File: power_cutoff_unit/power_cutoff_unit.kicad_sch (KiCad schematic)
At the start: 0 parts

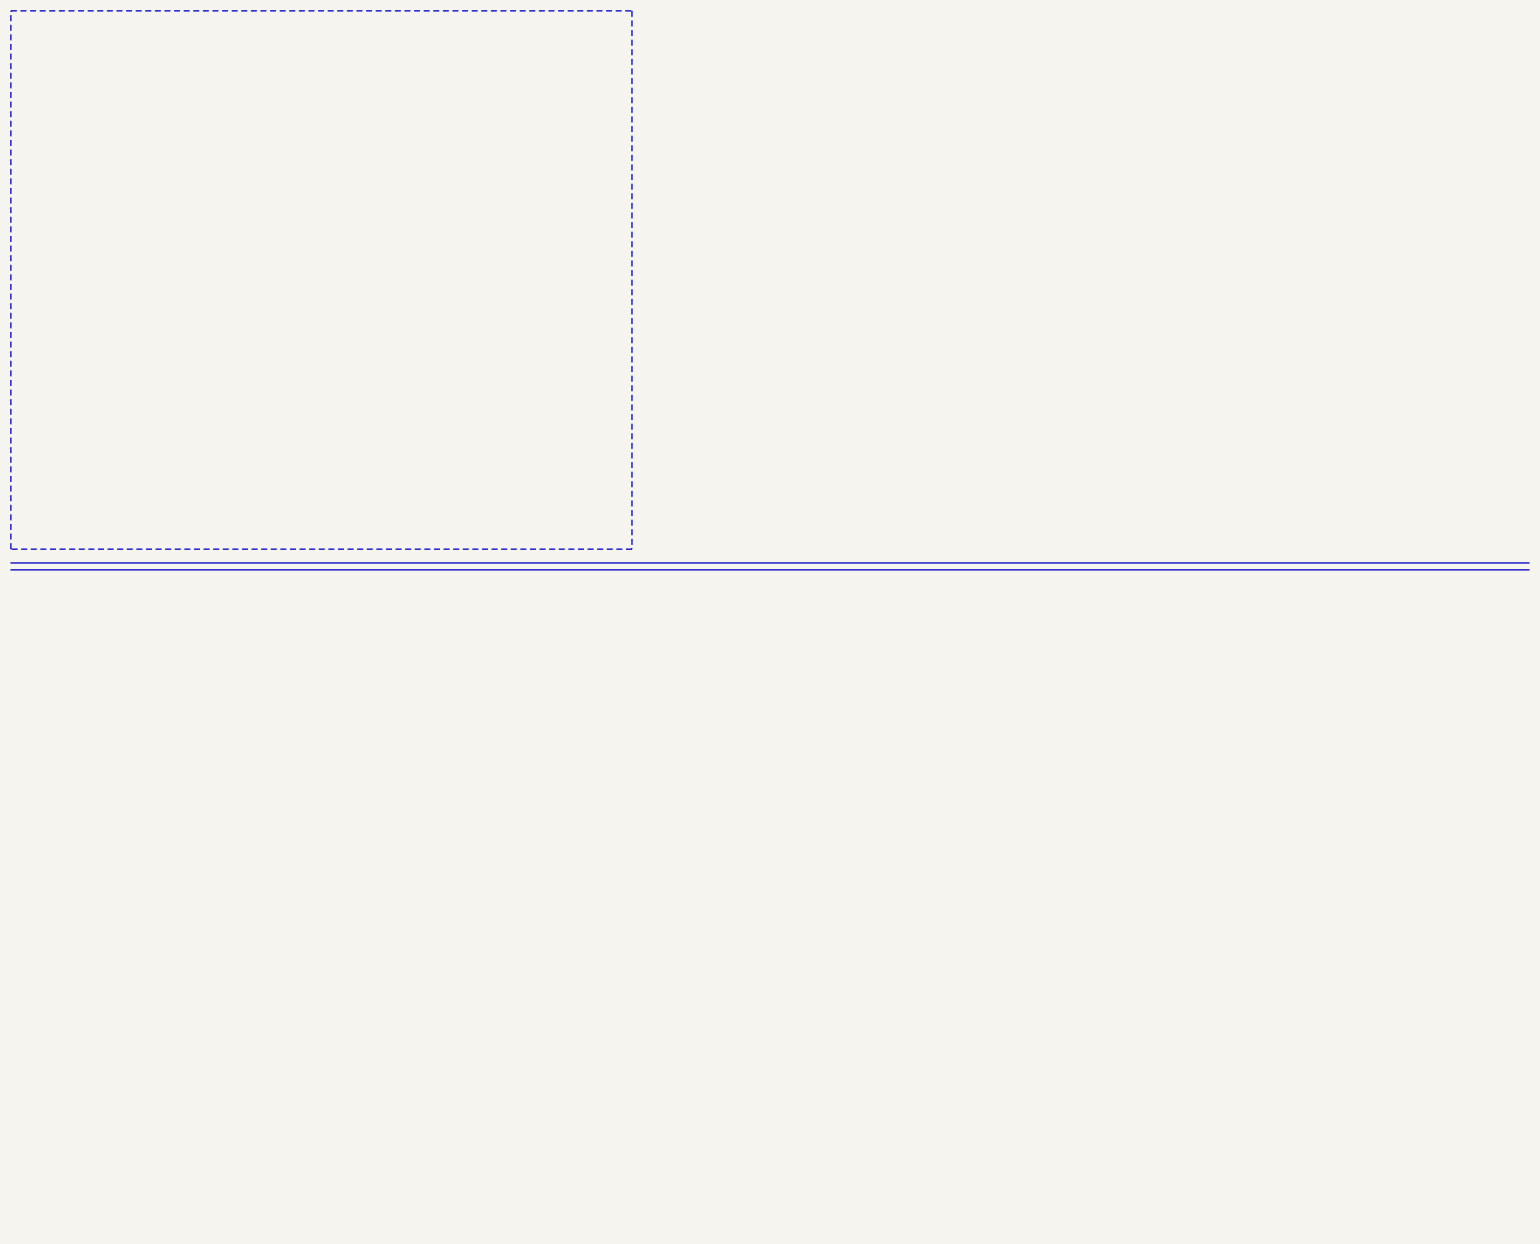
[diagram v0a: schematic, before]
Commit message: 集積回路だけ追加
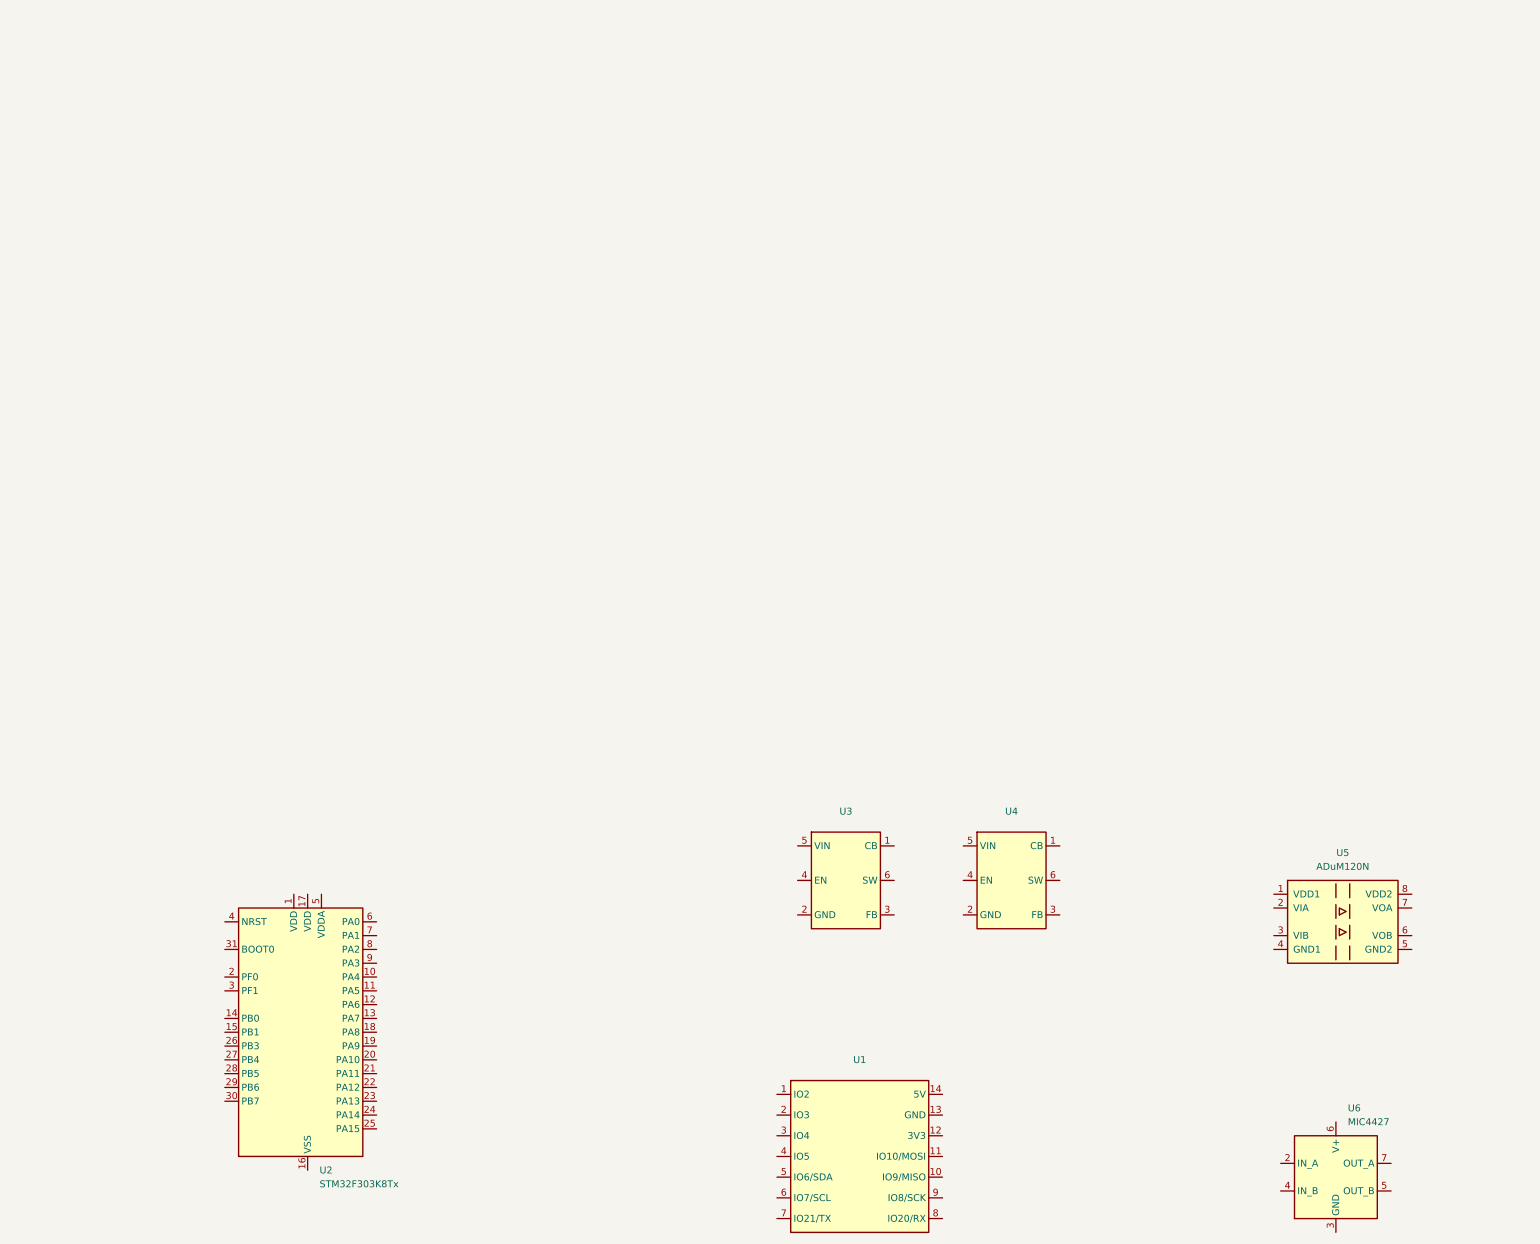
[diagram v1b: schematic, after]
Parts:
- added U1: ~, symbol Seed_XIAO:XIAO_ESP32C3
- added U2: STM32F303K8Tx, Package_QFP:LQFP-32_7x7mm_P0.8mm, symbol MCU_ST_STM32F3:STM32F303K8Tx
- added U3, U4: ~, symbol Power_Supply:LMR50410
- added U5: ADuM120N, Package_SO:SOIC-8_3.9x4.9mm_P1.27mm, symbol Isolator:ADuM120N
- added U6: MIC4427, symbol Driver_FET:MIC4427
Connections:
- new net: U2.16 (VSS), U2.32 (VSS)

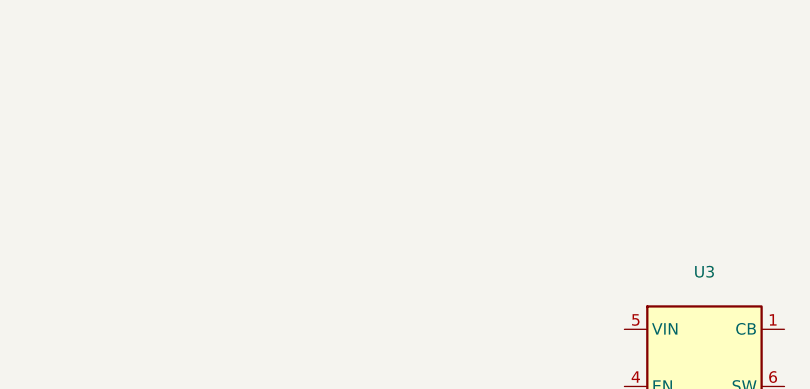
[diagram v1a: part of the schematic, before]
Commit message: 必要そうなシンボルとフットプリント追加
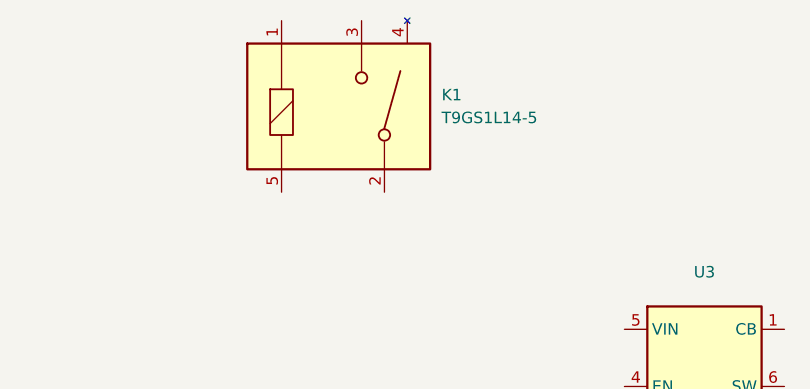
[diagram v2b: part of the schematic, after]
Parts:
- added K1: T9GS1L14-5, GN10_Relay:T9G, symbol GN10_Relay:T9GS1L14-5
- U1: footprint (none) -> RF_Module:MCU_Seeed_ESP32C3
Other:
- company: (none) -> TMCIT-Arakawa
- title: (none) -> GN10PowerCutoffUnit
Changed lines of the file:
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@@
 	(generator_version "8.0")
 	(paper "A3")
+	(title_block
+		(title "GN10PowerCutoffUnit")
+		(rev "v1.1")
+		(company "TMCIT-Arakawa")
+		(comment 1 "designed by Gento Aiba (GN10)")
+	)
 	(symbol
 		(lib_id "Power_Supply:LMR50410")
@@
 	)
 	(symbol
+		(lib_id "GN10_Relay:T9GS1L14-5")
+		(at 125.73 154.94 0)
+		(unit 1)
+		(exclude_from_sim no)
+		(in_bom yes)
+		(on_board yes)
+		(dnp no)
+		(fields_autoplaced yes)
+		(property "Reference" "K1"
+			(at 137.16 153.0349 0)
+			(effects
+				(font
+					(size 1.27 1.27)
+				)
+				(justify left)
+			)
+		)
+		(property "Value" "T9GS1L14-5"
+			(at 137.16 155.5749 0)
+			(effects
+				(font
+					(size 1.27 1.27)
+				)
+				(justify left)
+			)
+		)
+		(property "Footprint" "GN10_Relay:T9G"
+			(at 125.73 154.94 0)
+			(effects
+				(font
+					(size 1.27 1.27)
+				)
+				(hide yes)
+			)
+		)
+		(property "Datasheet" "https://www.mouser.jp/datasheet/2/418/8/ENG_DS_T9G_1216_0321-1281449.pdf"
+			(at 124.206 169.672 0)
+			(effects
+				(font
+					(size 1.27 1.27)
+				)
+				(hide yes)
+			)
+		)
+		(property "Description" "https://www.mouser.jp/ProductDetail/TE-Connectivity-PB/T9GS1L14-5?qs=gt1LBUVyoHmKCzoNwQtXUg%3D%3D&utm_id=21508984536&gad_source=1&gclid=Cj0KCQjw3vO3BhCqARIsAEWblcCBTCmY0mdqIVBL_wKnwWvKvQN3984iiMdI4LmBFLpfd6hpW_9dBrEaAue2EALw_wcB"
+			(at 123.952 171.704 0)
+			(effects
+				(font
+					(size 1.27 1.27)
+				)
+				(hide yes)
+			)
+		)
+		(pin "2"
+		)
+		(pin "4"
+		)
+		(pin "5"
+		)
+		(pin "1"
+		)
+		(pin "3"
+		)
+		(instances
+			(project ""
+				(path "/24fe50da-72e0-4baa-9f8a-567f58795612"
+					(reference "K1")
+					(unit 1)
+				)
+			)
+		)
+	)
+	(symbol
 		(lib_id "MCU_ST_STM32F3:STM32F303K8Tx")
 		(at 64.77 213.36 0)
@@
 			)
 		)
-		(property "Footprint" ""
+		(property "Footprint" "RF_Module:MCU_Seeed_ESP32C3"
 			(at 162.56 231.14 0)
 			(effects

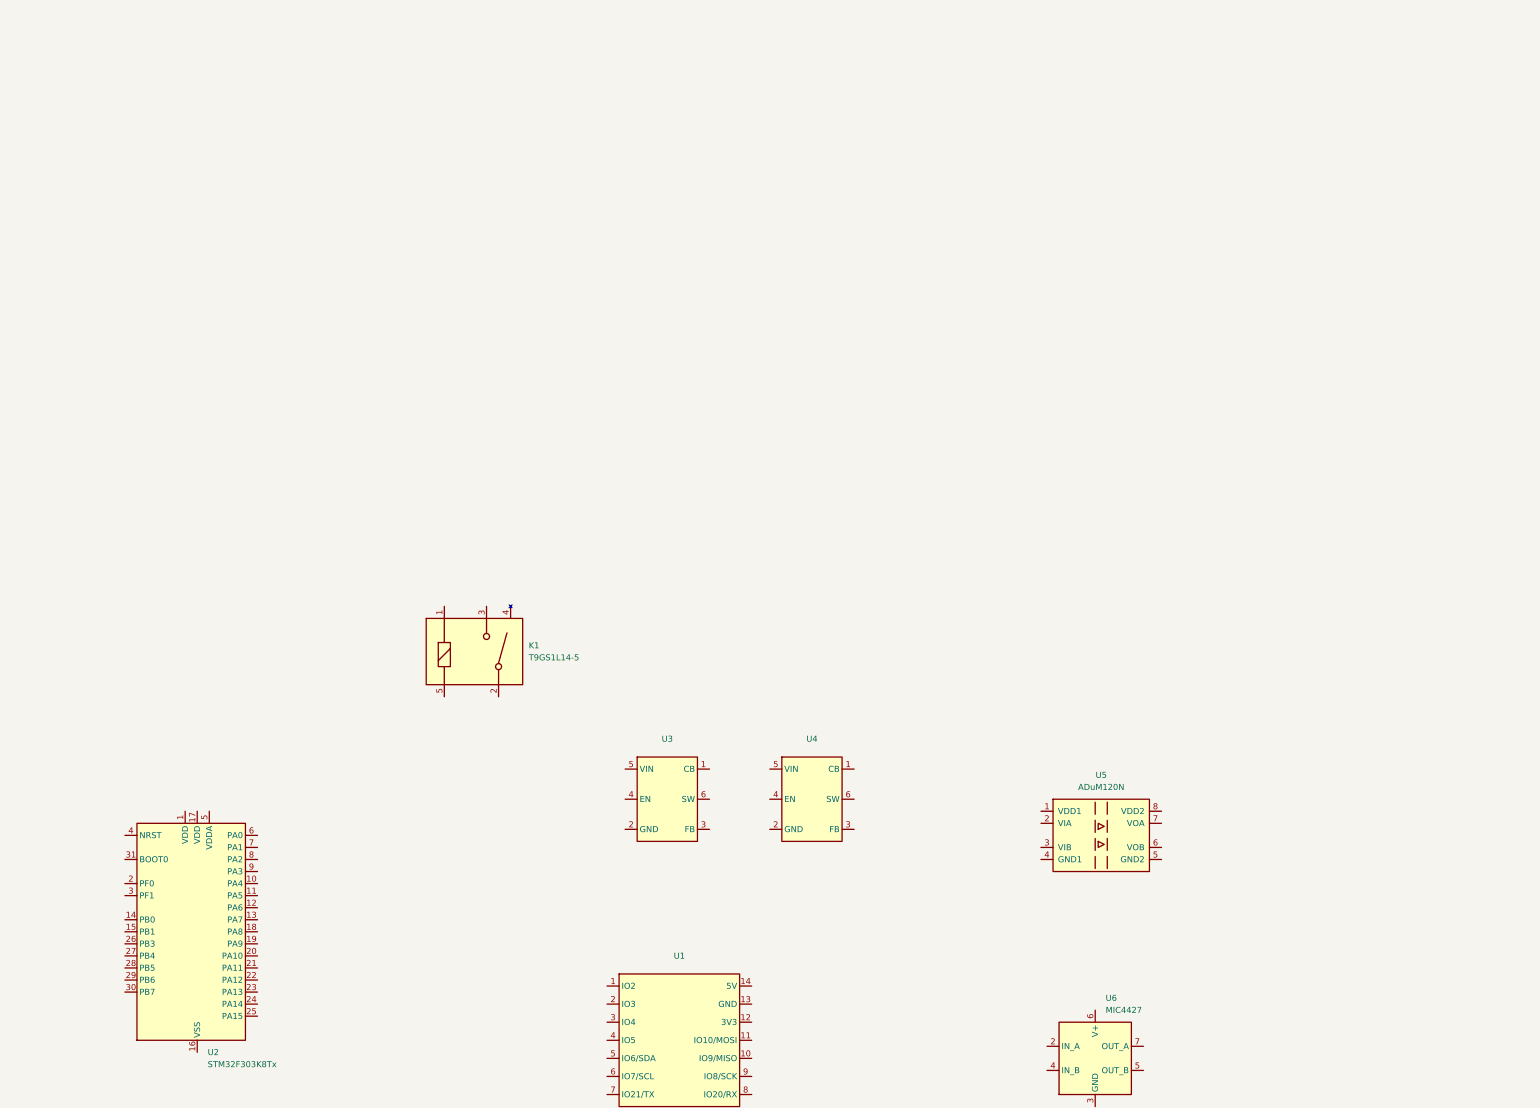
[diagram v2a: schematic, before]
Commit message: 電源回りの回路をいい加減に作った。
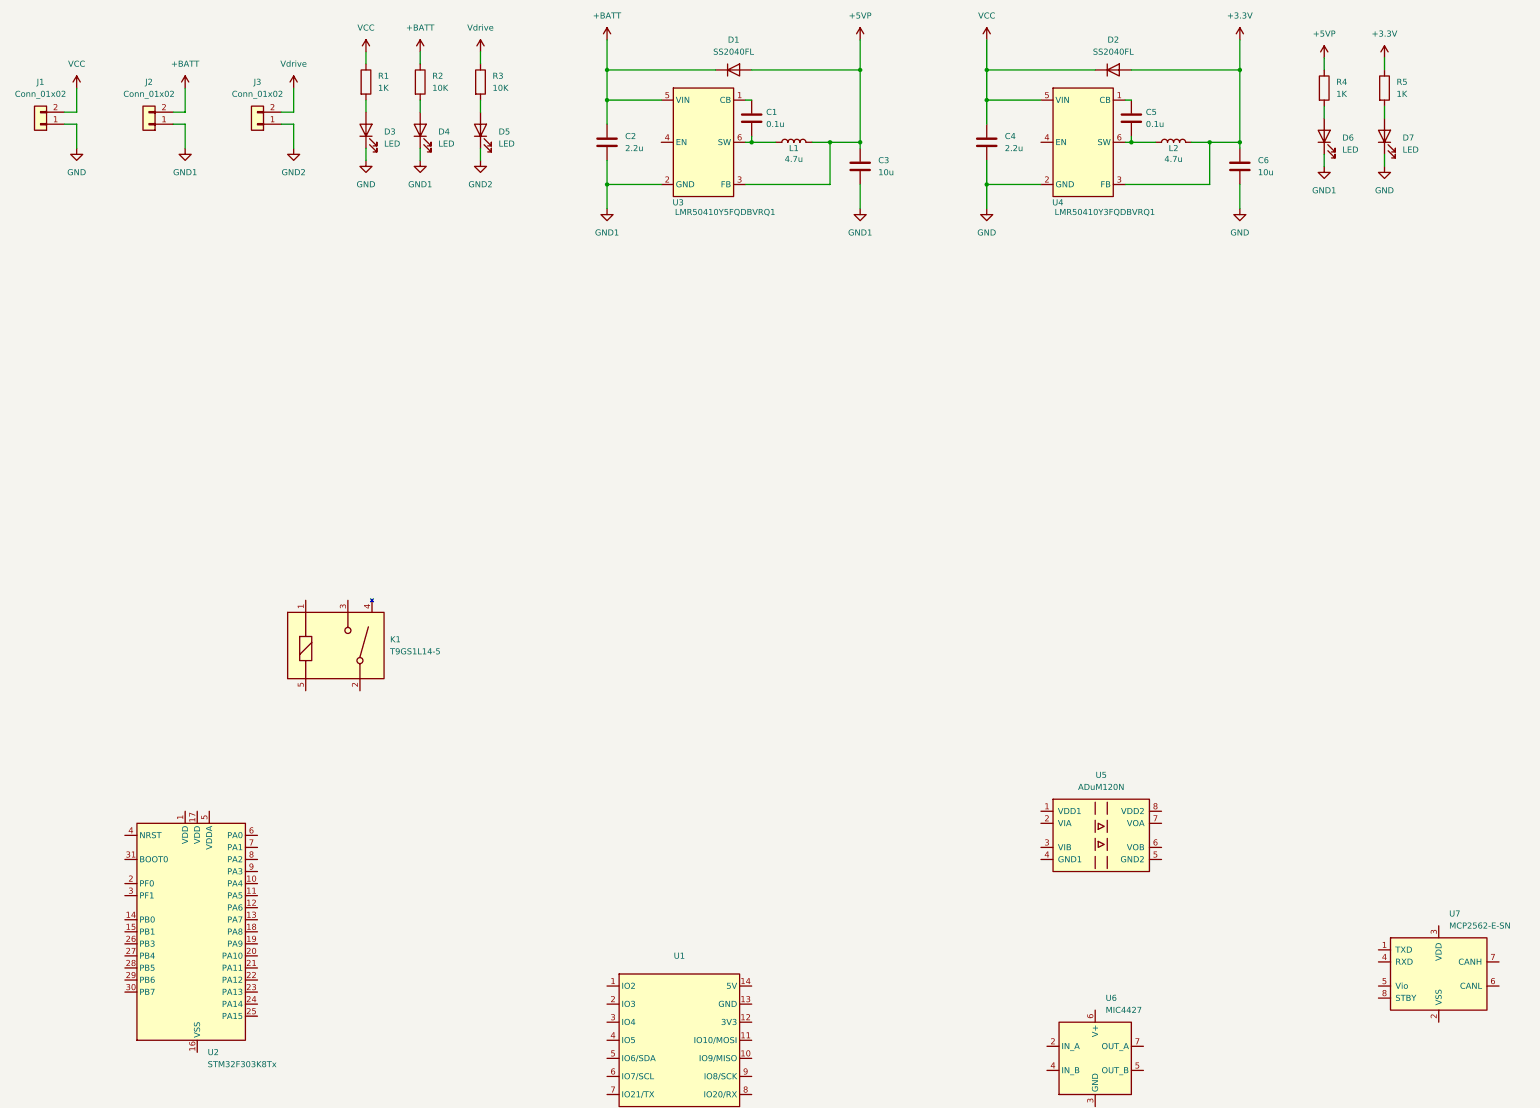
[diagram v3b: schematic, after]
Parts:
- added C1, C5: 0.1u, Capacitor_SMD:C_0402_1005Metric, symbol Device:C
- added C2, C4: 2.2u, symbol Device:C
- added C3, C6: 10u, symbol Device:C
- added D1, D2: SS2040FL, symbol Device:D
- added D3, D4, D5, D6, D7: LED, symbol Device:LED
- added J1, J2, J3: Conn_01x02, symbol Connector_Generic:Conn_01x02
- added L1, L2: 4.7u, symbol Device:L
- added R1, R4, R5: 1K, symbol Device:R
- added R2, R3: 10K, symbol Device:R
- added U7: MCP2562-E-SN, Package_SO:SOIC-8_3.9x4.9mm_P1.27mm, symbol Interface_CAN_LIN:MCP2562-E-SN
- K1: footprint GN10_Relay:T9G -> (none)
- U3: value ~ -> LMR50410Y5FQDBVRQ1; footprint (none) -> Package_TO_SOT_SMD:SOT-23-6
- U4: value ~ -> LMR50410Y3FQDBVRQ1; footprint (none) -> Package_TO_SOT_SMD:SOT-23-6
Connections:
- net at U4.1 (CB): now also C5.1
- net GND: now reaches U4.2 (GND)
- net GND: now also C4.2, C6.2, D3.1 (K), D7.1 (K), J1.1 (Pin_1)
- net +3.3V: now reaches U4.3 (FB)
- net +3.3V: now also C6.1, D2.2 (A), L2.2, R5.1
- net VCC: now reaches U4.5 (VIN)
- net VCC: now also C4.1, D2.1 (K), J1.2 (Pin_2), R1.1
- net at U4.6 (SW): now also C5.2, L2.1
- net at U3.1 (CB): now also C1.1
- net GND1: now reaches U3.2 (GND)
- net GND1: now also C2.2, C3.2, D4.1 (K), D6.1 (K), J2.1 (Pin_1)
- net +5VP: now reaches U3.3 (FB)
- net +5VP: now also C3.1, D1.2 (A), L1.2, R4.1
- net +BATT: now reaches U3.5 (VIN)
- net +BATT: now also C2.1, D1.1 (K), J2.2 (Pin_2), R2.1
- net at U3.6 (SW): now also C1.2, L1.1
- new net: D5.2 (A), R3.2
- new net: D7.2 (A), R5.2
- new net: D4.2 (A), R2.2
- new net: D3.2 (A), R1.2
- new net: D6.2 (A), R4.2
- new net GND2: D5.1 (K), J3.1 (Pin_1)
- new net Vdrive: J3.2 (Pin_2), R3.1
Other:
- moved on the sheet: K1, U3
